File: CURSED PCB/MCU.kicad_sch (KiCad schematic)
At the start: 22 parts, among them U1 STM32G431KBT6, U3 MIC94090YC6, Y1 24MHz crystal

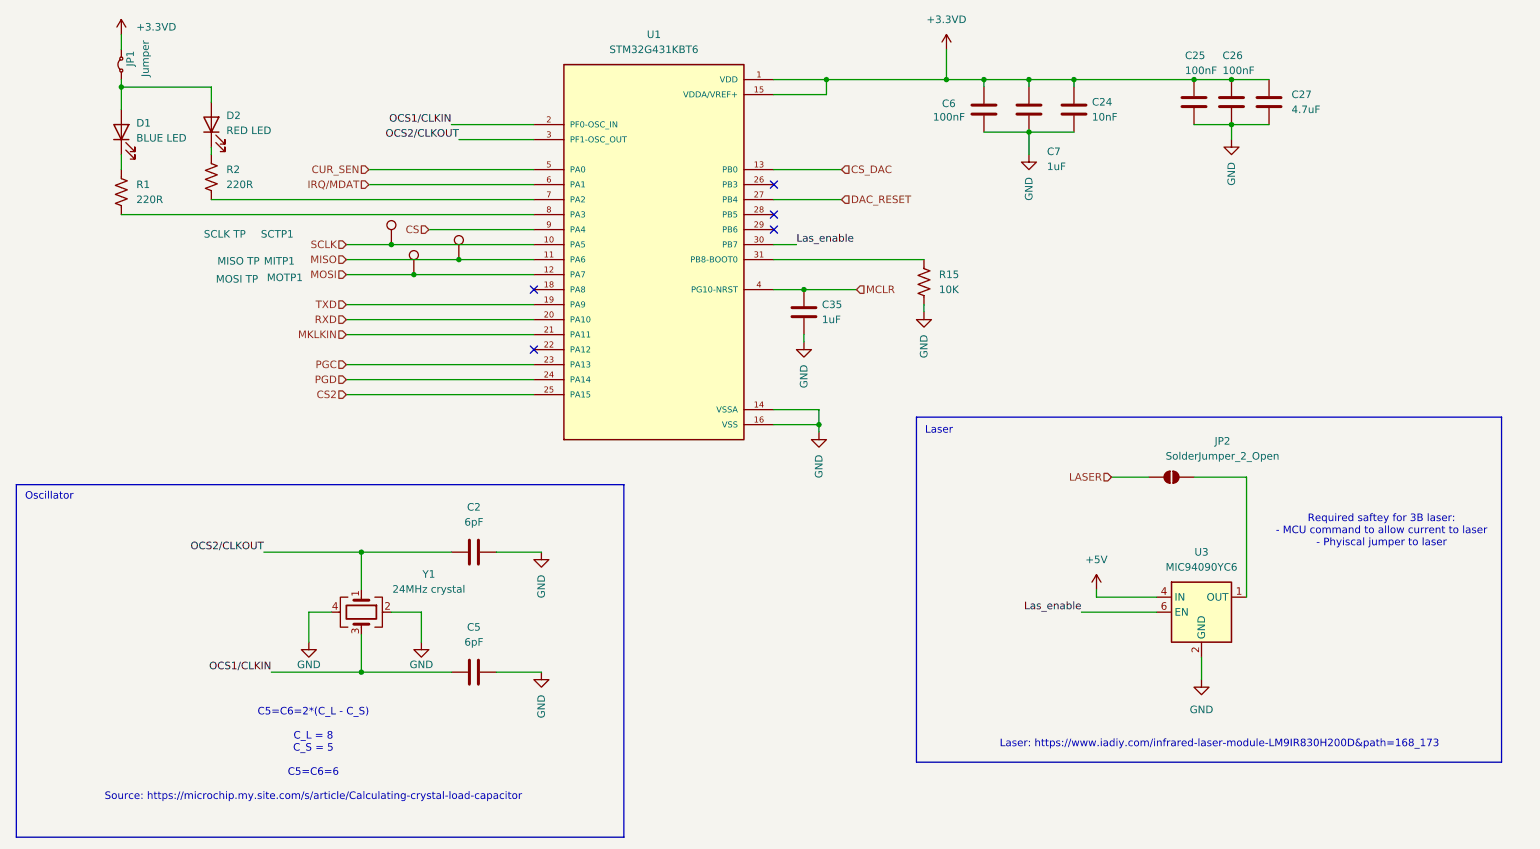
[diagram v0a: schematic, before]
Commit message: fixes from ash review
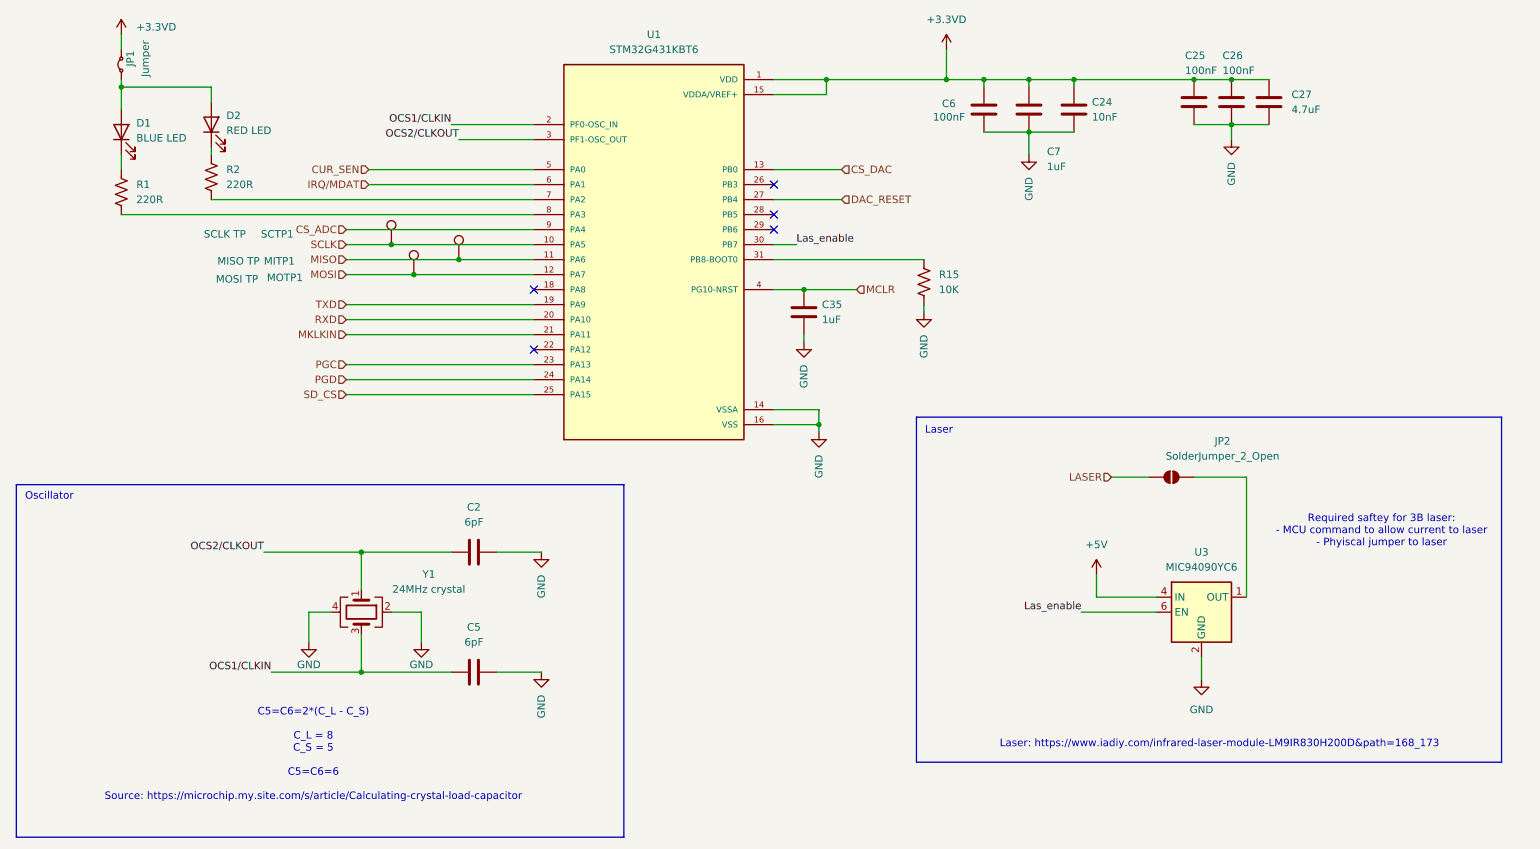
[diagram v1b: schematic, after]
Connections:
- net CS renamed CS_ADC
- net CS2 renamed SD_CS
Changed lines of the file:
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@@
 	(wire
 		(pts
-			(xy 204.47 134.62) (xy 204.47 133.35)
+			(xy 204.47 134.62) (xy 204.47 130.81)
 		)
 		(stroke
@@
 	(wire
 		(pts
-			(xy 91.44 72.39) (xy 109.22 72.39)
+			(xy 77.47 72.39) (xy 109.22 72.39)
 		)
 		(stroke
@@
 		)
 	)
-	(hierarchical_label "CS2"
+	(hierarchical_label "SD_CS"
 		(shape input)
 		(at 77.47 100.33 180)
@@
 		)
 	)
-	(hierarchical_label "CS"
+	(hierarchical_label "CS_ADC"
 		(shape input)
-		(at 91.44 72.39 180)
+		(at 77.47 72.39 180)
 		(effects
 			(font
@@
 	(symbol
 		(lib_id "power:+3.3VA")
-		(at 204.47 133.35 0)
+		(at 204.47 130.81 0)
 		(unit 1)
 		(exclude_from_sim no)
@@
 		(fields_autoplaced yes)
 		(property "Reference" "#PWR015"
-			(at 204.47 137.16 0)
+			(at 204.47 134.62 0)
 			(effects
 				(font
@@
 		)
 		(property "Value" "+5V"
-			(at 204.47 128.27 0)
+			(at 204.47 125.73 0)
 			(effects
 				(font
@@
 		)
 		(property "Footprint" ""
-			(at 204.47 133.35 0)
+			(at 204.47 130.81 0)
 			(effects
 				(font
@@
 		)
 		(property "Datasheet" ""
-			(at 204.47 133.35 0)
+			(at 204.47 130.81 0)
 			(effects
 				(font
@@
 		)
 		(property "Description" "Power symbol creates a global label with name \"+3.3VA\""
-			(at 204.47 133.35 0)
-			(effects
-				(font
+			(at 204.47 130.81 0)
+			(effects
+				(font
